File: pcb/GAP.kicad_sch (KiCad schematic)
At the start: 103 parts, among them J1 USB_C_Receptacle, J2 Conn_01x02_Pin, J3 Conn_01x06_Socket, J4 Conn_01x05_Socket, Q1 BSP613, Q2 2N7002E, Q3 2N7002E, Q4 2N7002E, Q5 2N7002E, Q6 2N7002E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

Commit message: Change SW10 library
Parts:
- SW10: footprint Button_Switch_SMD:SW_SPDT_CK-JS102011SAQN -> Button_Switch_SMD:SW_SPDT_CK_JS102011SAQN
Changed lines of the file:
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@@
       (effects (font (size 1.27 1.27)) hide)
     )
-    (property "Footprint" "Button_Switch_SMD:SW_SPDT_CK-JS102011SAQN" (at 156.845 46.99 0)
+    (property "Footprint" "Button_Switch_SMD:SW_SPDT_CK_JS102011SAQN" (at 156.845 46.99 0)
       (effects (font (size 1.27 1.27)) hide)
     )

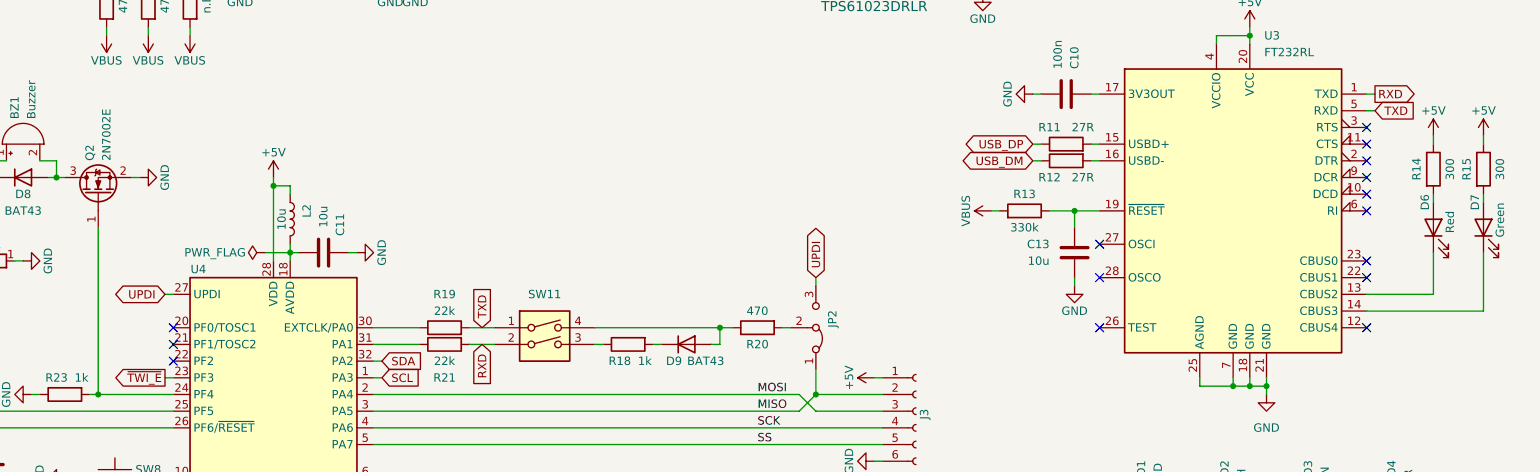
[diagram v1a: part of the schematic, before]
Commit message: Add RTS/CTS to UART interface
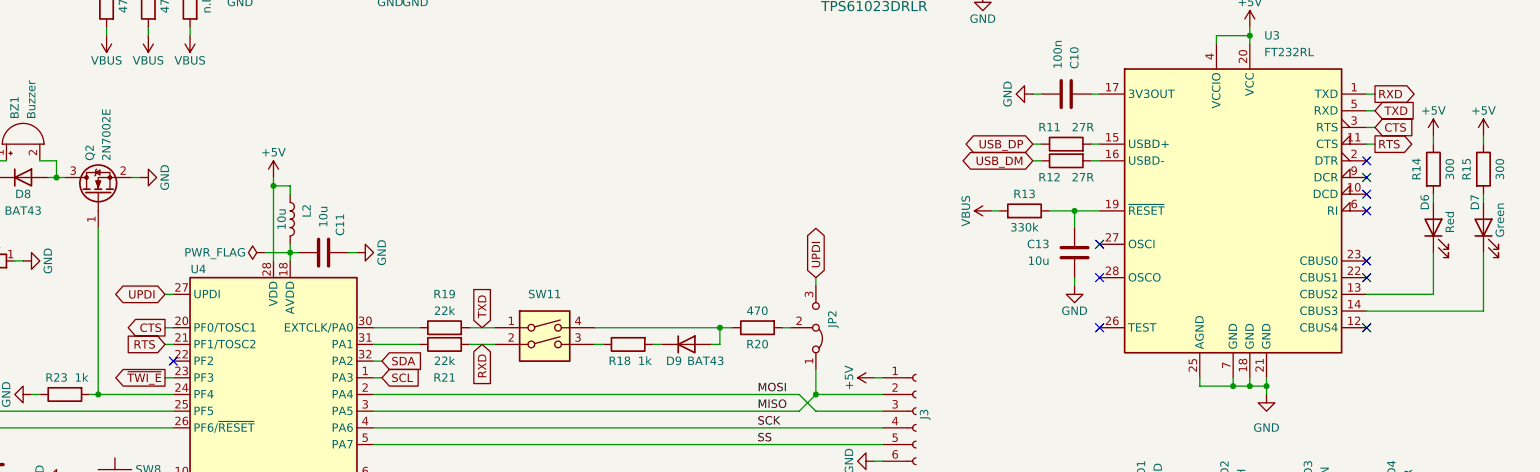
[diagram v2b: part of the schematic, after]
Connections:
- net RTS: now reaches U3.11 (CTS)
- net RTS: now also U4.21 (PF1/TOSC2)
- net CTS: now reaches U3.3 (RTS)
- net CTS: now also U4.20 (PF0/TOSC1)
- no-connect marks 17 -> 13
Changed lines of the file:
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@@
   (no_connect (at 248.92 88.9))
   (no_connect (at 248.92 91.44))
-  (no_connect (at 67.31 114.3))
-  (no_connect (at 248.92 83.82))
-  (no_connect (at 67.31 111.76))
   (no_connect (at 248.92 93.98))
   (no_connect (at 41.91 55.88))
@@
   (no_connect (at 248.92 111.76))
   (no_connect (at 208.28 104.14))
-  (no_connect (at 248.92 81.28))
   (no_connect (at 208.28 99.06))
   (no_connect (at 248.92 104.14))
@@
     (stroke (width 0) (type default))
   )
+  (wire (pts (xy 66.04 111.76) (xy 67.31 111.76))
+    (stroke (width 0) (type default))
+  )
   (wire (pts (xy 160.02 111.76) (xy 161.29 111.76))
     (stroke (width 0) (type default))
@@
     (stroke (width 0) (type default))
   )
+  (wire (pts (xy 66.04 114.3) (xy 67.31 114.3))
+    (stroke (width 0) (type default))
+  )
   (wire (pts (xy 190.5 59.69) (xy 190.5 60.96))
     (stroke (width 0) (type default))
@@
     (stroke (width 0) (type default))
   )
+  (wire (pts (xy 248.92 81.28) (xy 250.19 81.28))
+    (stroke (width 0) (type default))
+  )
   (wire (pts (xy 46.99 121.92) (xy 45.72 121.92))
     (stroke (width 0) (type default))
@@
   )
   (wire (pts (xy 43.18 160.02) (xy 43.18 158.75))
+    (stroke (width 0) (type default))
+  )
+  (wire (pts (xy 248.92 83.82) (xy 250.19 83.82))
     (stroke (width 0) (type default))
   )
@@
     )
   )
+  (global_label "CTS" (shape output) (at 66.04 111.76 180) (fields_autoplaced)
+    (effects (font (size 1.27 1.27)) (justify right))
+    (property "Intersheetrefs" "${INTERSHEET_REFS}" (at 59.6077 111.76 0)
+      (effects (font (size 1.27 1.27)) (justify right) hide)
+    )
+  )
   (global_label "RXD" (shape input) (at 114.3 114.3 270) (fields_autoplaced)
     (effects (font (size 1.27 1.27)) (justify right))
@@
     )
   )
+  (global_label "RTS" (shape output) (at 250.19 83.82 0) (fields_autoplaced)
+    (effects (font (size 1.27 1.27)) (justify left))
+    (property "Intersheetrefs" "${INTERSHEET_REFS}" (at 256.6223 83.82 0)
+      (effects (font (size 1.27 1.27)) (justify left) hide)
+    )
+  )
   (global_label "USB_DM" (shape bidirectional) (at 44.45 39.37 0) (fields_autoplaced)
     (effects (font (size 1.27 1.27)) (justify left))
@@
     )
   )
+  (global_label "CTS" (shape input) (at 250.19 81.28 0) (fields_autoplaced)
+    (effects (font (size 1.27 1.27)) (justify left))
+    (property "Intersheetrefs" "${INTERSHEET_REFS}" (at 256.6223 81.28 0)
+      (effects (font (size 1.27 1.27)) (justify left) hide)
+    )
+  )
+  (global_label "RTS" (shape input) (at 66.04 114.3 180) (fields_autoplaced)
+    (effects (font (size 1.27 1.27)) (justify right))
+    (property "Intersheetrefs" "${INTERSHEET_REFS}" (at 59.6077 114.3 0)
+      (effects (font (size 1.27 1.27)) (justify right) hide)
+    )
+  )

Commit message: Change partlist vendors
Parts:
- F1: Vendor DigiKey -> HTL; VendorId NANOSMDC200F-2CT-ND -> 103597
- F2: Vendor DigiKey -> HTL; VendorId NANOSMDC150F-2CT-ND -> 103598
- FB1: Vendor DigiKey -> HTL; VendorId 2512067007Y3 -> 103570
- J1: Vendor DigiKey -> HTL; VendorId 2073-USB4110-GF-A-1-ND -> 103572
- J2: Vendor DigiKey -> HTL; VendorId 455-1719-ND -> 103599
- L1: Vendor DigiKey -> HTL; VendorId 587-2890-1-ND -> 103600
- L2: Vendor DigiKey -> HTL; VendorId 541-2607-1-ND -> 103574
- Q1: Vendor DigiKey -> HTL; VendorId BSP613PH6327XTSA1CT-ND -> 103601
- R1: Vendor DigiKey -> HTL; VendorId 311-732KFRCT-ND -> 103602
- R16, R17: Vendor DigiKey -> HTL; VendorId RMCF1206FT5K10CT-ND -> 102962
- SW10: Vendor DigiKey -> HTL; VendorId 401-1999-1-ND -> 103603
- SW11: Vendor DigiKey -> HTL; VendorId CT2192LPST-ND -> 103604
- U1: Vendor DigiKey -> HTL; VendorId MCP73833T-AMI/UNCT-ND -> 103605
- U2: Vendor DigiKey -> HTL; VendorId 296-TPS61023DRLRCT-ND -> 103606
- U4: Vendor DigiKey -> HTL; VendorId 150-ATMEGA4808-AURCT-ND -> 103582
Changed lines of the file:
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@@
       (effects (font (size 1.27 1.27)) hide)
     )
-    (property "Vendor" "DigiKey" (at 119.38 58.42 0)
+    (property "Vendor" "HTL" (at 119.38 58.42 0)
       (effects (font (size 1.27 1.27)) hide)
     )
-    (property "VendorId" "455-1719-ND" (at 119.38 58.42 0)
+    (property "VendorId" "103599" (at 119.38 58.42 0)
       (effects (font (size 1.27 1.27)) hide)
     )
@@
       (effects (font (size 1.27 1.27)) hide)
     )
-    (property "Vendor" "DigiKey" (at 26.67 40.64 0)
+    (property "Vendor" "HTL" (at 26.67 40.64 0)
       (effects (font (size 1.27 1.27)) hide)
     )
-    (property "VendorId" "2073-USB4110-GF-A-1-ND" (at 26.67 40.64 0)
+    (property "VendorId" "103572" (at 26.67 40.64 0)
       (effects (font (size 1.27 1.27)) hide)
     )
@@
       (effects (font (size 1.27 1.27)) hide)
     )
-    (property "Vendor" "DigiKey" (at 156.845 46.99 0)
+    (property "Vendor" "HTL" (at 156.845 46.99 0)
       (effects (font (size 1.27 1.27)) hide)
     )
-    (property "VendorId" "401-1999-1-ND" (at 156.845 46.99 0)
+    (property "VendorId" "103603" (at 156.845 46.99 0)
       (effects (font (size 1.27 1.27)) hide)
     )
@@
       (effects (font (size 1.27 1.27)) hide)
     )
-    (property "Vendor" "DigiKey" (at 123.825 114.3 0)
+    (property "Vendor" "HTL" (at 123.825 114.3 0)
       (effects (font (size 1.27 1.27)) hide)
     )
-    (property "VendorId" "CT2192LPST-ND" (at 123.825 114.3 0)
+    (property "VendorId" "103604" (at 123.825 114.3 0)
       (effects (font (size 1.27 1.27)) hide)
     )
@@
       (effects (font (size 1.27 1.27)) hide)
     )
-    (property "Vendor" "DigiKey" (at 190.5 43.18 0)
+    (property "Vendor" "HTL" (at 190.5 43.18 0)
       (effects (font (size 1.27 1.27)) hide)
     )
-    (property "VendorId" "311-732KFRCT-ND" (at 190.5 43.18 0)
+    (property "VendorId" "103602" (at 190.5 43.18 0)
       (effects (font (size 1.27 1.27)) hide)
     )
@@
       (effects (font (size 1.27 1.27)) hide)
     )
-    (property "Vendor" "DigiKey" (at 71.12 25.4 0)
+    (property "Vendor" "HTL" (at 71.12 25.4 0)
       (effects (font (size 1.27 1.27)) hide)
     )
-    (property "VendorId" "NANOSMDC200F-2CT-ND" (at 71.12 25.4 0)
+    (property "VendorId" "103597" (at 71.12 25.4 0)
       (effects (font (size 1.27 1.27)) hide)
     )
@@
       (effects (font (size 1.27 1.27) italic) hide)
     )
-    (property "Vendor" "DigiKey" (at 173.99 46.99 0)
+    (property "Vendor" "HTL" (at 173.99 46.99 0)
       (effects (font (size 1.27 1.27)) hide)
     )
-    (property "VendorId" "296-TPS61023DRLRCT-ND" (at 173.99 46.99 0)
+    (property "VendorId" "103606" (at 173.99 46.99 0)
       (effects (font (size 1.27 1.27)) hide)
     )
@@
       (effects (font (size 1.27 1.27)) hide)
     )
-    (property "Vendor" "DigiKey" (at 85.09 95.25 0)
+    (property "Vendor" "HTL" (at 85.09 95.25 0)
       (effects (font (size 1.27 1.27)) hide)
     )
-    (property "VendorId" "541-2607-1-ND" (at 85.09 95.25 0)
+    (property "VendorId" "103574" (at 85.09 95.25 0)
       (effects (font (size 1.27 1.27)) hide)
     )
@@
       (effects (font (size 1.27 1.27)) hide)
     )
-    (property "Vendor" "DigiKey" (at 46.99 30.48 0)
+    (property "Vendor" "HTL" (at 46.99 30.48 0)
       (effects (font (size 1.27 1.27)) hide)
     )
-    (property "VendorId" "RMCF1206FT5K10CT-ND" (at 46.99 30.48 0)
+    (property "VendorId" "102962" (at 46.99 30.48 0)
       (effects (font (size 1.27 1.27)) hide)
     )
@@
       (effects (font (size 1.27 1.27)) hide)
     )
-    (property "Vendor" "DigiKey" (at 125.73 35.56 0)
+    (property "Vendor" "HTL" (at 125.73 35.56 0)
       (effects (font (size 1.27 1.27)) hide)
     )
-    (property "VendorId" "BSP613PH6327XTSA1CT-ND" (at 125.73 35.56 0)
+    (property "VendorId" "103601" (at 125.73 35.56 0)
       (effects (font (size 1.27 1.27)) hide)
     )
@@
       (effects (font (size 1.27 1.27)) hide)
     )
-    (property "Vendor" "DigiKey" (at 119.38 46.99 0)
+    (property "Vendor" "HTL" (at 119.38 46.99 0)
       (effects (font (size 1.27 1.27)) hide)
     )
-    (property "VendorId" "NANOSMDC150F-2CT-ND" (at 119.38 46.99 0)
+    (property "VendorId" "103598" (at 119.38 46.99 0)
       (effects (font (size 1.27 1.27)) hide)
     )
@@
       (effects (font (size 1.27 1.27)) hide)
     )
-    (property "Vendor" "DigiKey" (at 46.99 33.02 0)
+    (property "Vendor" "HTL" (at 46.99 33.02 0)
       (effects (font (size 1.27 1.27)) hide)
     )
-    (property "VendorId" "RMCF1206FT5K10CT-ND" (at 46.99 33.02 0)
+    (property "VendorId" "102962" (at 46.99 33.02 0)
       (effects (font (size 1.27 1.27)) hide)
     )
@@
       (effects (font (size 1.27 1.27)) hide)
     )
-    (property "Vendor" "DigiKey" (at 82.55 129.54 0)
+    (property "Vendor" "HTL" (at 82.55 129.54 0)
       (effects (font (size 1.27 1.27)) hide)
     )
-    (property "VendorId" "150-ATMEGA4808-AURCT-ND" (at 82.55 129.54 0)
+    (property "VendorId" "103582" (at 82.55 129.54 0)
       (effects (font (size 1.27 1.27)) hide)
     )
@@
       (effects (font (size 1.27 1.27)) hide)
     )
-    (property "Vendor" "DigiKey" (at 88.9 43.18 0)
+    (property "Vendor" "HTL" (at 88.9 43.18 0)
       (effects (font (size 1.27 1.27)) hide)
     )
-    (property "VendorId" "MCP73833T-AMI/UNCT-ND" (at 88.9 43.18 0)
+    (property "VendorId" "103605" (at 88.9 43.18 0)
       (effects (font (size 1.27 1.27)) hide)
     )
@@
       (effects (font (size 1.27 1.27)) hide)
     )
-    (property "Vendor" "DigiKey" (at 62.23 25.4 0)
+    (property "Vendor" "HTL" (at 62.23 25.4 0)
       (effects (font (size 1.27 1.27)) hide)
     )
-    (property "VendorId" "2512067007Y3" (at 62.23 25.4 0)
+    (property "VendorId" "103570" (at 62.23 25.4 0)
       (effects (font (size 1.27 1.27)) hide)
     )
@@
       (effects (font (size 1.27 1.27)) hide)
     )
-    (property "Vendor" "DigiKey" (at 173.99 38.1 0)
+    (property "Vendor" "HTL" (at 173.99 38.1 0)
       (effects (font (size 1.27 1.27)) hide)
     )
-    (property "VendorId" "587-2890-1-ND" (at 173.99 38.1 0)
+    (property "VendorId" "103600" (at 173.99 38.1 0)
       (effects (font (size 1.27 1.27)) hide)
     )
